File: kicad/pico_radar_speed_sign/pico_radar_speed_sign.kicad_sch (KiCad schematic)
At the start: 29 parts, among them J1 Conn_02x08_Odd_Even, J2 Conn_02x08_Odd_Even, J3 Conn_01x02, J4 Conn_01x03_Pin, J5 Conn_01x04, U1 Pico_H, U2 74HC595, U3 74HC595, U5 LM2596S-ADJ

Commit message: Make Pico controller Rev A
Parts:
- added C5: DNP, Capacitor_SMD:C_0805_2012Metric, symbol Device:C
- added J6: 2.00mm JST-PH 01x03, Connector_JST:JST_PH_B3B-PH-K_1x03_P2.00mm_Vertical, symbol Connector:Conn_01x03_Pin
- C1, C2: LCSC MPN (none) -> C49678; MPN (none) -> CC0805KRX7R9BB104; Standard Cost (none) -> 0.01
- C3: LCSC MPN (none) -> C88725
- C4: LCSC MPN (none) -> C88729
- J1, J2: value Conn_02x08_Odd_Even -> 0.1" Pin Header 02x08; LCSC MPN (none) -> C492436; MPN (none) -> PZ254R-12-16P; Standard Cost (none) -> 0.05
- J3: value Conn_01x02 -> 5.08mm Terminal Block 01x02; LCSC MPN (none) -> C8465; MPN (none) -> WJ500V-5.08-2P; Standard Cost (none) -> 0.06
- J4: value Conn_01x03_Pin -> 0.1" Pin Header 01x03; LCSC MPN (none) -> C492411; MPN (none) -> PZ254R-11-03P; Standard Cost (none) -> 0.01
- J5: value Conn_01x04 -> 2.54mm Terminal Block 01x04; LCSC MPN (none) -> C915913; MPN (none) -> XY308-2.54-4P; Standard Cost (none) -> 0.21
- L1: LCSC MPN (none) -> C182153
- PART1, PART2: value Part -> 0.1" Pin Socket 01x20; LCSC MPN (none) -> C2897383; MPN (none) -> PM254-1-20-Z-8.5; Standard Cost (none) -> 0.16
- R1, R2, R3, R5: LCSC MPN (none) -> C84376; MPN (none) -> RC0805FR-0710KL; Standard Cost (none) -> 0.01
- R4: LCSC MPN (none) -> C126352; MPN (none) -> RC0805FR-0730KL; Standard Cost (none) -> 0.01
- U1: MPN (none) -> SC0917; Standard Cost (none) -> 5.00
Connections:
- net +5V: now also C5.1, J6.2 (Pin_2)
- net DOPPLER_RADAR_IN: now also J4.3 (Pin_3), U1.34 (GPIO28_ADC2), J6.3 (Pin_3); no longer J4.1 (Pin_1), U1.1 (GPIO0)
- net GND: now also J4.1 (Pin_1), J6.1 (Pin_1); no longer J4.3 (Pin_3)
- net at R4.2, R5.1, U5.4 (FB): now also C5.2
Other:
- note added: "C_ff"
- company: (none) -> Pants for Birds
- title: (none) -> Pi Pico Radar Speed Sign Controller
- moved on the sheet: C1, C2, C4, J1, J2, J4, J5, PART1, PART2, R1, R2, R3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

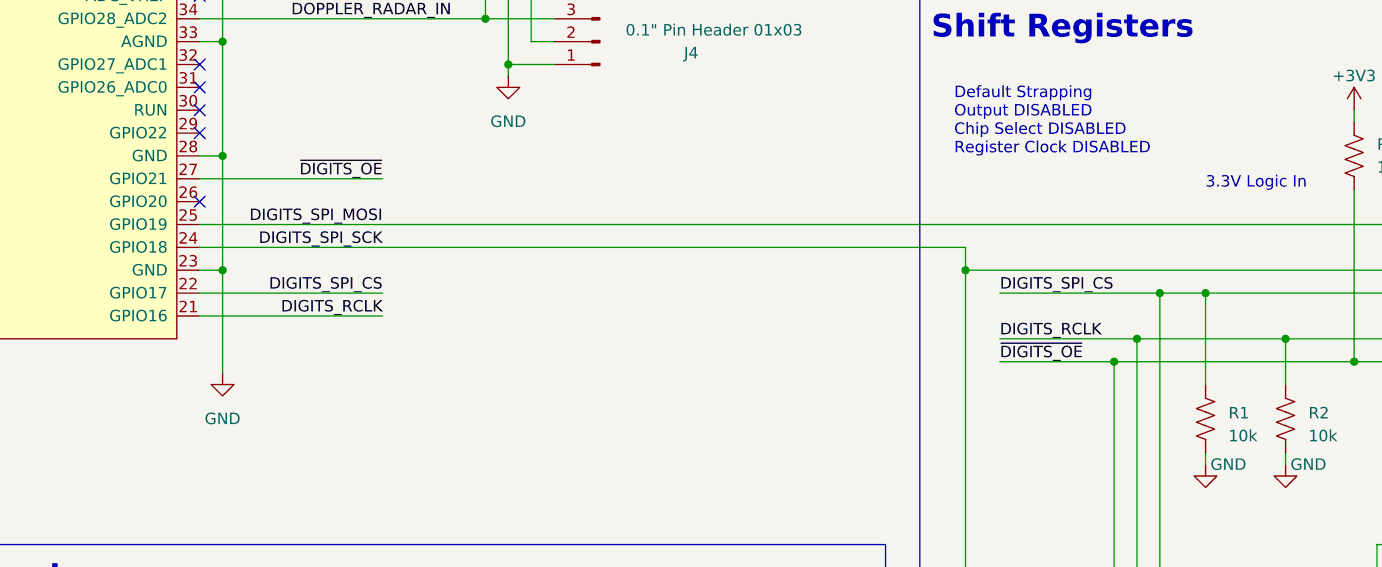
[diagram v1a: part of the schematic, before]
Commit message: Add demo mode to display code
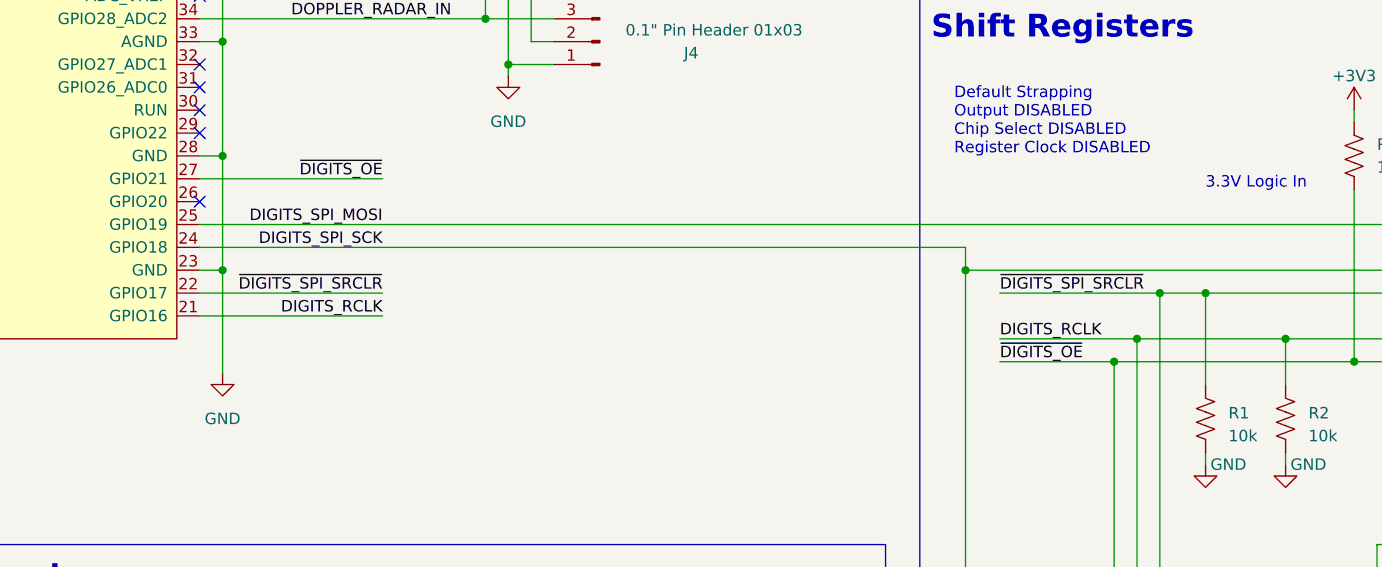
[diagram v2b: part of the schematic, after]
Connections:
- net DIGITS_SPI_CS renamed ~{DIGITS_SPI_SRCLR}
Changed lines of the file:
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@@
     (effects (font (size 1.27 1.27)) (justify left bottom))
   )
-  (label "DIGITS_SPI_CS" (at 200.66 80.01 0) (fields_autoplaced)
+  (label "~{DIGITS_SPI_SRCLR}" (at 200.66 80.01 0) (fields_autoplaced)
     (effects (font (size 1.27 1.27)) (justify left bottom))
   )
@@
     (effects (font (size 1.27 1.27)) (justify left bottom))
   )
-  (label "DIGITS_SPI_CS" (at 132.08 80.01 180) (fields_autoplaced)
+  (label "~{DIGITS_SPI_SRCLR}" (at 132.08 80.01 180) (fields_autoplaced)
     (effects (font (size 1.27 1.27)) (justify right bottom))
   )

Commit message: Make Rev C of segen seg, update README
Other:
- note added: "TODO: fix radar input!!"
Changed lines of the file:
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@@
     (effects (font (size 1.27 1.27)) (justify right bottom))
+  )
+  (text "TODO: fix radar input!!" (at 157.48 83.82 0)
+    (effects (font (size 1.27 1.27)) (justify left bottom))
   )
   (text "C_ff" (at 146.0302 142.2034 0)
